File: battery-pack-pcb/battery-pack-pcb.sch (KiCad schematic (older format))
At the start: 7 parts, among them J1 Conn_01x02_Female, J2 Conn_01x02_Female

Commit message: Add capacitor to battery pack
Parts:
- D1, D2: symbol Device:D_Small -> Device:D_Schottky_Small
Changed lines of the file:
@@
 $EndComp
 $Comp
-L Device:D_Small D1
+L Device:D_Schottky_Small D1
 U 1 1 5D5C10F0
 P 3500 2500
@@
 $EndComp
 $Comp
-L Device:D_Small D2
+L Device:D_Schottky_Small D2
 U 1 1 5D5C26DF
 P 4400 2500

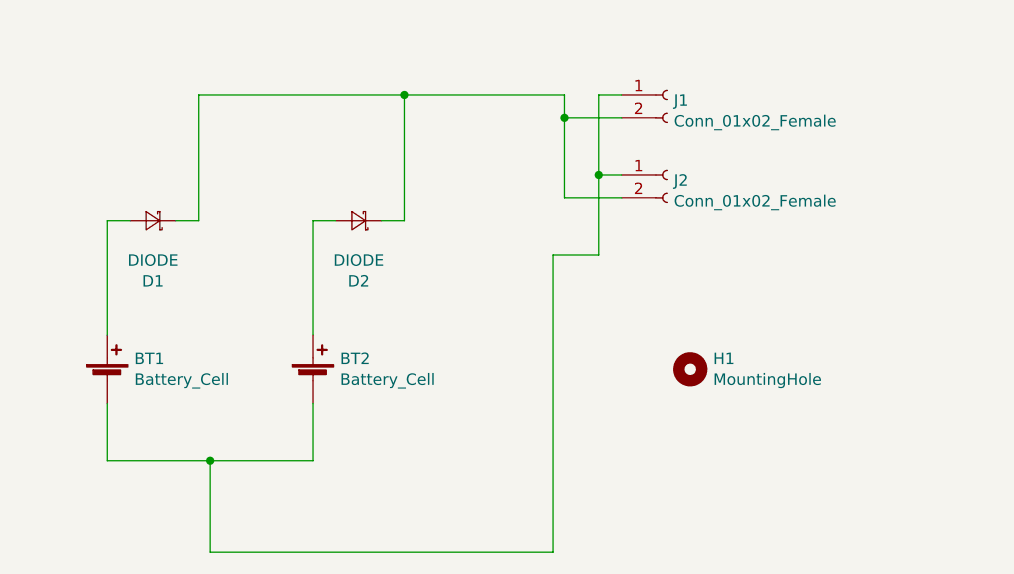
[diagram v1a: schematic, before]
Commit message: Delete regulator
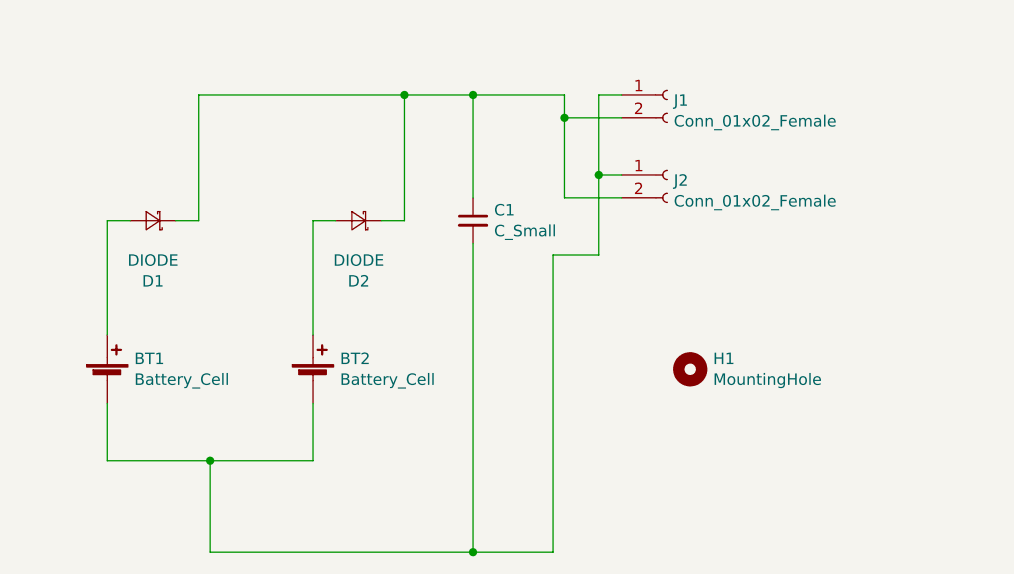
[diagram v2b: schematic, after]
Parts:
- added C1: C_Small, Capacitor_SMD:C_1210_3225Metric_Pad1.42x2.65mm_HandSolder, symbol Device:C_Small
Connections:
- net at BT1.2 (-), BT2.2 (-), J1.1 (Pin_1)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: now also C1.2
- net at D1.1 (K), D2.1 (K), J1.2 (Pin_2)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: now also C1.1
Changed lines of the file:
@@
 	3750 3550 3750 3950
 Wire Wire Line
-	3750 3950 5250 3950
+	3750 3950 4900 3950
 Connection ~ 3750 3550
 Wire Wire Line
@@
 $EndComp
 Wire Wire Line
-	4600 1950 5300 1950
+	4600 1950 4900 1950
 Wire Wire Line
 	5300 1950 5300 2050
@@
 Wire Wire Line
 	4500 2500 4600 2500
+$Comp
+L Device:C_Small C1
+U 1 1 5D987608
+P 4900 2500
+F 0 "C1" H 4992 2546 50  0000 L CNN
+F 1 "C_Small" H 4992 2455 50  0000 L CNN
+F 2 "Capacitor_SMD:C_1210_3225Metric_Pad1.42x2.65mm_HandSolder" H 4900 2500 50  0001 C CNN
+F 3 "~" H 4900 2500 50  0001 C CNN
+	1    4900 2500
+	1    0    0    -1
+$EndComp
+Wire Wire Line
+	4900 1950 4900 2400
+Connection ~ 4900 1950
+Wire Wire Line
+	4900 1950 5300 1950
+Wire Wire Line
+	4900 2600 4900 3950
+Connection ~ 4900 3950
+Wire Wire Line
+	4900 3950 5250 3950
 $EndSCHEMATC

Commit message: Update silk of battery pack pcb
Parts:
- J1, J2: footprint Connector_JST:JST_PH_S2B-PH-K_1x02_P2.00mm_Horizontal -> locallib:JST_PH_S2B-PH-K_1x02_P2.00mm_Horizontal_nosilk
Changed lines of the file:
@@
 F 0 "J1" H 5778 1926 50  0000 L CNN
 F 1 "Conn_01x02_Female" H 5778 1835 50  0000 L CNN
-F 2 "Connector_JST:JST_PH_S2B-PH-K_1x02_P2.00mm_Horizontal" H 5750 1950 50  0001 C CNN
+F 2 "locallib:JST_PH_S2B-PH-K_1x02_P2.00mm_Horizontal_nosilk" H 5750 1950 50  0001 C CNN
 F 3 "~" H 5750 1950 50  0001 C CNN
 	1    5750 1950
@@
 F 0 "J2" H 5778 2276 50  0000 L CNN
 F 1 "Conn_01x02_Female" H 5778 2185 50  0000 L CNN
-F 2 "Connector_JST:JST_PH_S2B-PH-K_1x02_P2.00mm_Horizontal" H 5750 2300 50  0001 C CNN
+F 2 "locallib:JST_PH_S2B-PH-K_1x02_P2.00mm_Horizontal_nosilk" H 5750 2300 50  0001 C CNN
 F 3 "~" H 5750 2300 50  0001 C CNN
 	1    5750 2300

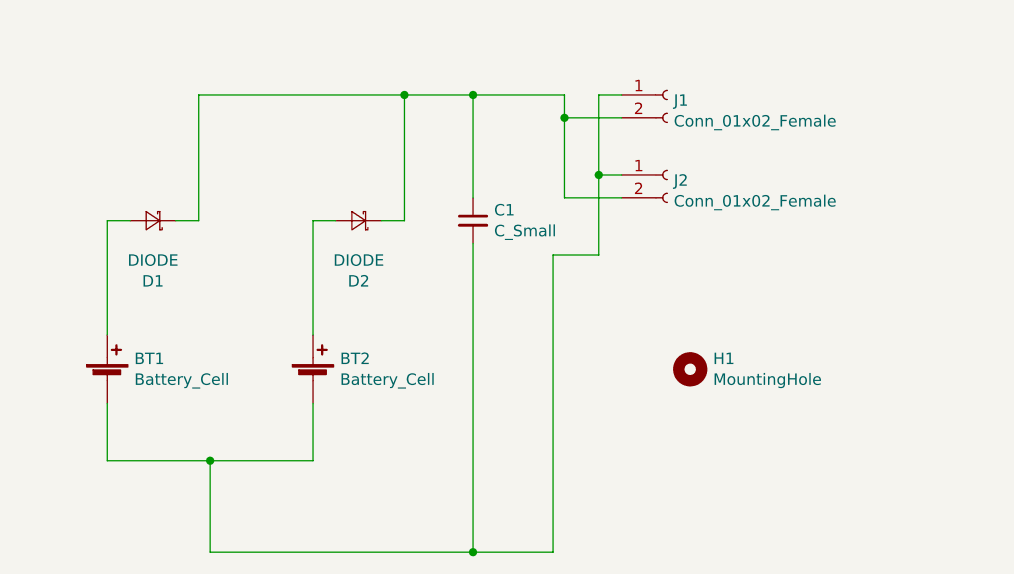
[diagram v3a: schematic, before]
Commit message: Add power switch to battery PCB
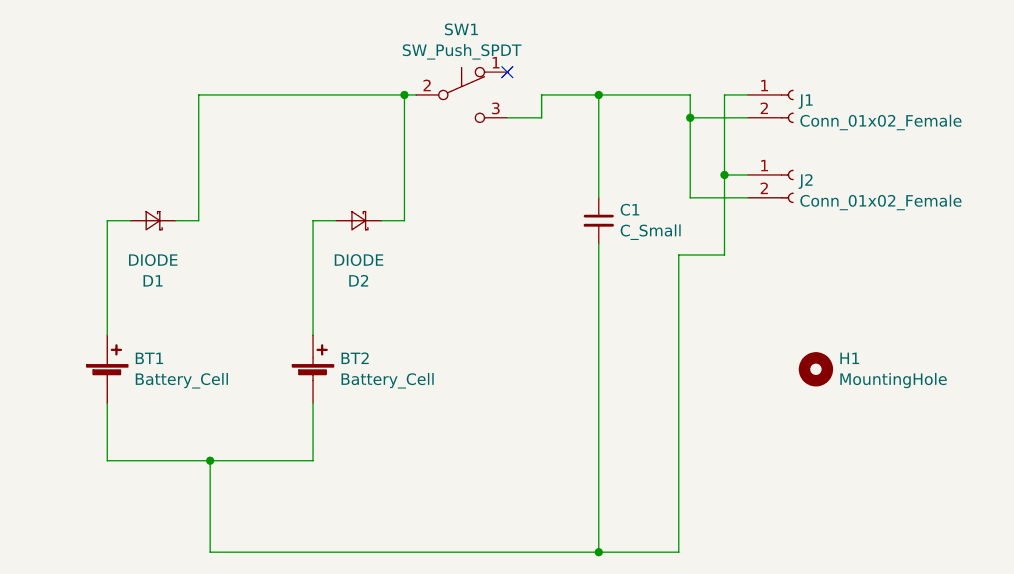
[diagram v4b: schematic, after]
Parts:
- added SW1: SW_Push_SPDT, locallib:slide_switch_vertical_01x03_pitch2mm, symbol Switch:SW_Push_SPDT
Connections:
- net at C1.1, J1.2 (Pin_2), J2.2 (Pin_2): now also SW1.3 (C); no longer D1.1 (K), D2.1 (K)
- new net: D1.1 (K), D2.1 (K), SW1.2 (B)
- no-connect marks 0 -> 1
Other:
- moved on the sheet: C1, H1, J1, J2
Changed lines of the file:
@@
 Wire Wire Line
 	3750 3550 3750 3950
-Wire Wire Line
-	3750 3950 4900 3950
 Connection ~ 3750 3550
 Wire Wire Line
@@
 L Connector:Conn_01x02_Female J1
 U 1 1 5D5C4DA3
-P 5750 1950
-F 0 "J1" H 5778 1926 50  0000 L CNN
-F 1 "Conn_01x02_Female" H 5778 1835 50  0000 L CNN
-F 2 "locallib:JST_PH_S2B-PH-K_1x02_P2.00mm_Horizontal_nosilk" H 5750 1950 50  0001 C CNN
-F 3 "~" H 5750 1950 50  0001 C CNN
-	1    5750 1950
+P 6300 1950
+F 0 "J1" H 6328 1926 50  0000 L CNN
+F 1 "Conn_01x02_Female" H 6328 1835 50  0000 L CNN
+F 2 "locallib:JST_PH_S2B-PH-K_1x02_P2.00mm_Horizontal_nosilk" H 6300 1950 50  0001 C CNN
+F 3 "~" H 6300 1950 50  0001 C CNN
+	1    6300 1950
 	1    0    0    -1
 $EndComp
@@
 L Connector:Conn_01x02_Female J2
 U 1 1 5D5C5DA6
-P 5750 2300
-F 0 "J2" H 5778 2276 50  0000 L CNN
-F 1 "Conn_01x02_Female" H 5778 2185 50  0000 L CNN
-F 2 "locallib:JST_PH_S2B-PH-K_1x02_P2.00mm_Horizontal_nosilk" H 5750 2300 50  0001 C CNN
-F 3 "~" H 5750 2300 50  0001 C CNN
-	1    5750 2300
+P 6300 2300
+F 0 "J2" H 6328 2276 50  0000 L CNN
+F 1 "Conn_01x02_Female" H 6328 2185 50  0000 L CNN
+F 2 "locallib:JST_PH_S2B-PH-K_1x02_P2.00mm_Horizontal_nosilk" H 6300 2300 50  0001 C CNN
+F 3 "~" H 6300 2300 50  0001 C CNN
+	1    6300 2300
 	1    0    0    -1
 $EndComp
 Wire Wire Line
-	4600 1950 4900 1950
+	5850 1950 5850 2050
 Wire Wire Line
-	5300 1950 5300 2050
+	5850 2050 6100 2050
 Wire Wire Line
-	5300 2050 5550 2050
-Connection ~ 4600 1950
+	5850 2050 5850 2400
 Wire Wire Line
-	5300 2050 5300 2400
+	5850 2400 6100 2400
+Connection ~ 5850 2050
 Wire Wire Line
-	5300 2400 5550 2400
-Connection ~ 5300 2050
+	5800 3950 5800 2650
 Wire Wire Line
-	5250 3950 5250 2650
+	5800 2650 6000 2650
 Wire Wire Line
-	5250 2650 5450 2650
+	6000 2650 6000 2300
 Wire Wire Line
-	5450 2650 5450 2300
+	6000 2300 6100 2300
 Wire Wire Line
-	5450 2300 5550 2300
+	6000 2300 6000 1950
 Wire Wire Line
-	5450 2300 5450 1950
-Wire Wire Line
-	5450 1950 5550 1950
-Connection ~ 5450 2300
+	6000 1950 6100 1950
+Connection ~ 6000 2300
 $Comp
 L Mechanical:MountingHole H1
 U 1 1 5D5C3A45
-P 5850 3150
-F 0 "H1" H 5950 3196 50  0000 L CNN
-F 1 "MountingHole" H 5950 3105 50  0000 L CNN
-F 2 "MountingHole:MountingHole_2.2mm_M2" H 5850 3150 50  0001 C CNN
-F 3 "~" H 5850 3150 50  0001 C CNN
-	1    5850 3150
+P 6400 3150
+F 0 "H1" H 6500 3196 50  0000 L CNN
+F 1 "MountingHole" H 6500 3105 50  0000 L CNN
+F 2 "MountingHole:MountingHole_2.2mm_M2" H 6400 3150 50  0001 C CNN
+F 3 "~" H 6400 3150 50  0001 C CNN
+	1    6400 3150
 	1    0    0    -1
 $EndComp
@@
 L Device:C_Small C1
 U 1 1 5D987608
-P 4900 2500
-F 0 "C1" H 4992 2546 50  0000 L CNN
-F 1 "C_Small" H 4992 2455 50  0000 L CNN
-F 2 "Capacitor_SMD:C_1210_3225Metric_Pad1.42x2.65mm_HandSolder" H 4900 2500 50  0001 C CNN
-F 3 "~" H 4900 2500 50  0001 C CNN
-	1    4900 2500
+P 5450 2500
+F 0 "C1" H 5542 2546 50  0000 L CNN
+F 1 "C_Small" H 5542 2455 50  0000 L CNN
+F 2 "Capacitor_SMD:C_1210_3225Metric_Pad1.42x2.65mm_HandSolder" H 5450 2500 50  0001 C CNN
+F 3 "~" H 5450 2500 50  0001 C CNN
+	1    5450 2500
 	1    0    0    -1
 $EndComp
 Wire Wire Line
-	4900 1950 4900 2400
-Connection ~ 4900 1950
+	5450 1950 5450 2400
 Wire Wire Line
-	4900 1950 5300 1950
+	5450 1950 5850 1950
 Wire Wire Line
-	4900 2600 4900 3950
-Connection ~ 4900 3950
+	5450 2600 5450 3950
+Connection ~ 5450 3950
 Wire Wire Line
-	4900 3950 5250 3950
+	5450 3950 5800 3950
+$Comp
+L Switch:SW_Push_SPDT SW1
+U 1 1 5DCF88DF
+P 4850 1950
+F 0 "SW1" H 4850 2235 50  0000 C CNN
+F 1 "SW_Push_SPDT" H 4850 2144 50  0000 C CNN
+F 2 "locallib:slide_switch_vertical_01x03_pitch2mm" H 4850 1950 50  0001 C CNN
+F 3 "~" H 4850 1950 50  0001 C CNN
+	1    4850 1950
+	1    0    0    -1
+$EndComp
+Wire Wire Line
+	4650 1950 4600 1950
+Connection ~ 4600 1950
+Wire Wire Line
+	3750 3950 5450 3950
+NoConn ~ 5050 1850
+Wire Wire Line
+	5050 2050 5200 2050
+Wire Wire Line
+	5200 2050 5200 1950
+Wire Wire Line
+	5200 1950 5450 1950
+Connection ~ 5450 1950
 $EndSCHEMATC
